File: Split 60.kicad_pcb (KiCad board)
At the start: 2 copper layers, 173 x 106.4 mm, 175 parts, among them SW1 SW_Push, SW2 SW_Push, U1 ATmega32U4-AU, U2 ATmega32U4-AU, Y1 16MHz, Y2 16MHz

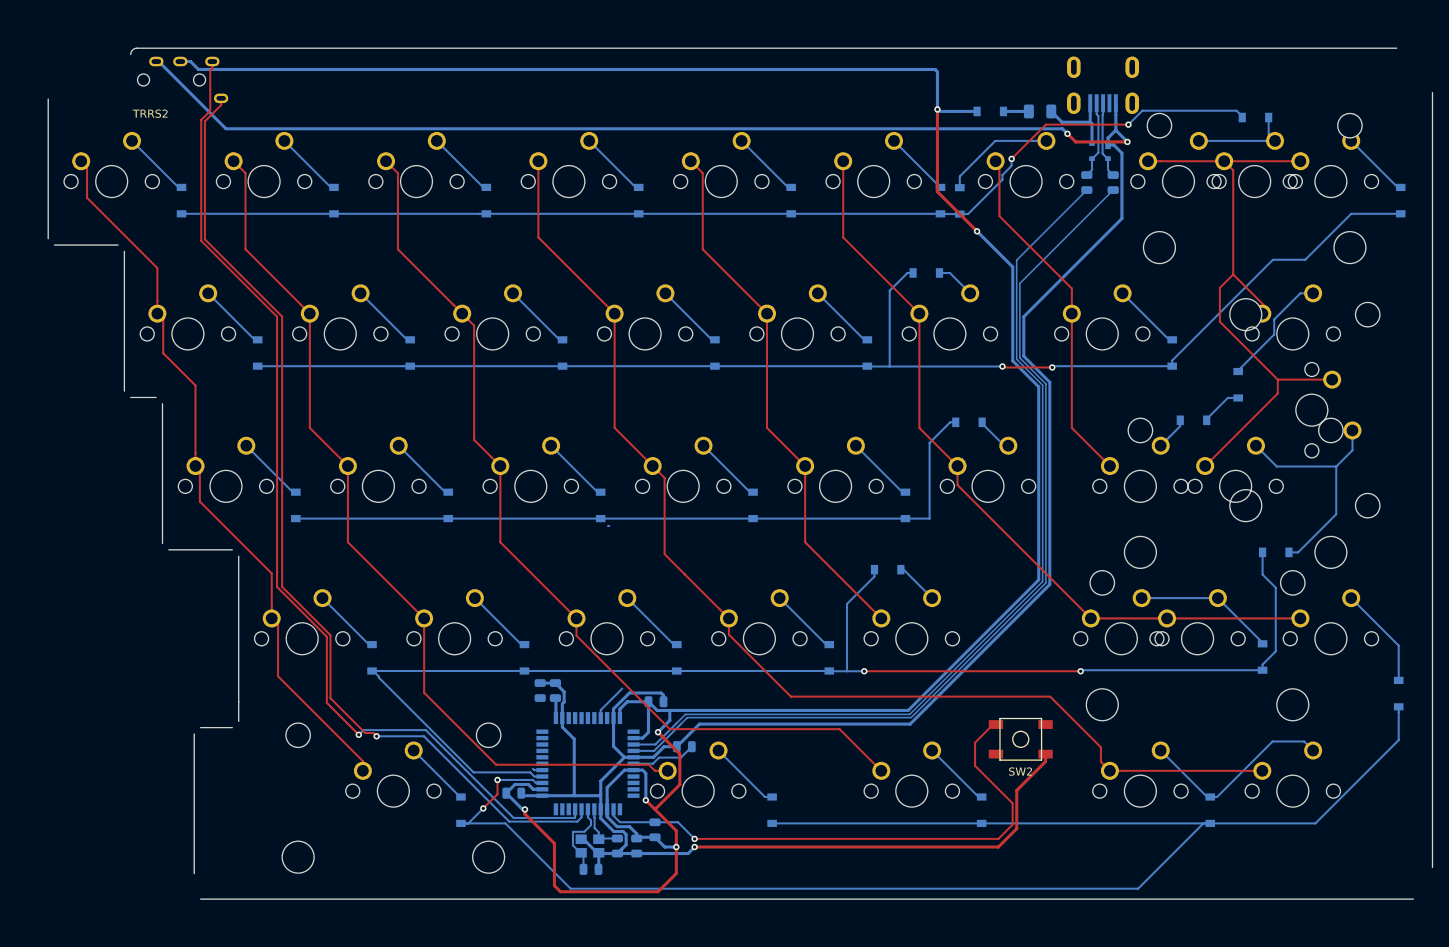
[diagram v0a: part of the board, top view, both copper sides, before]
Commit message: Rename to split 60, tweak routing
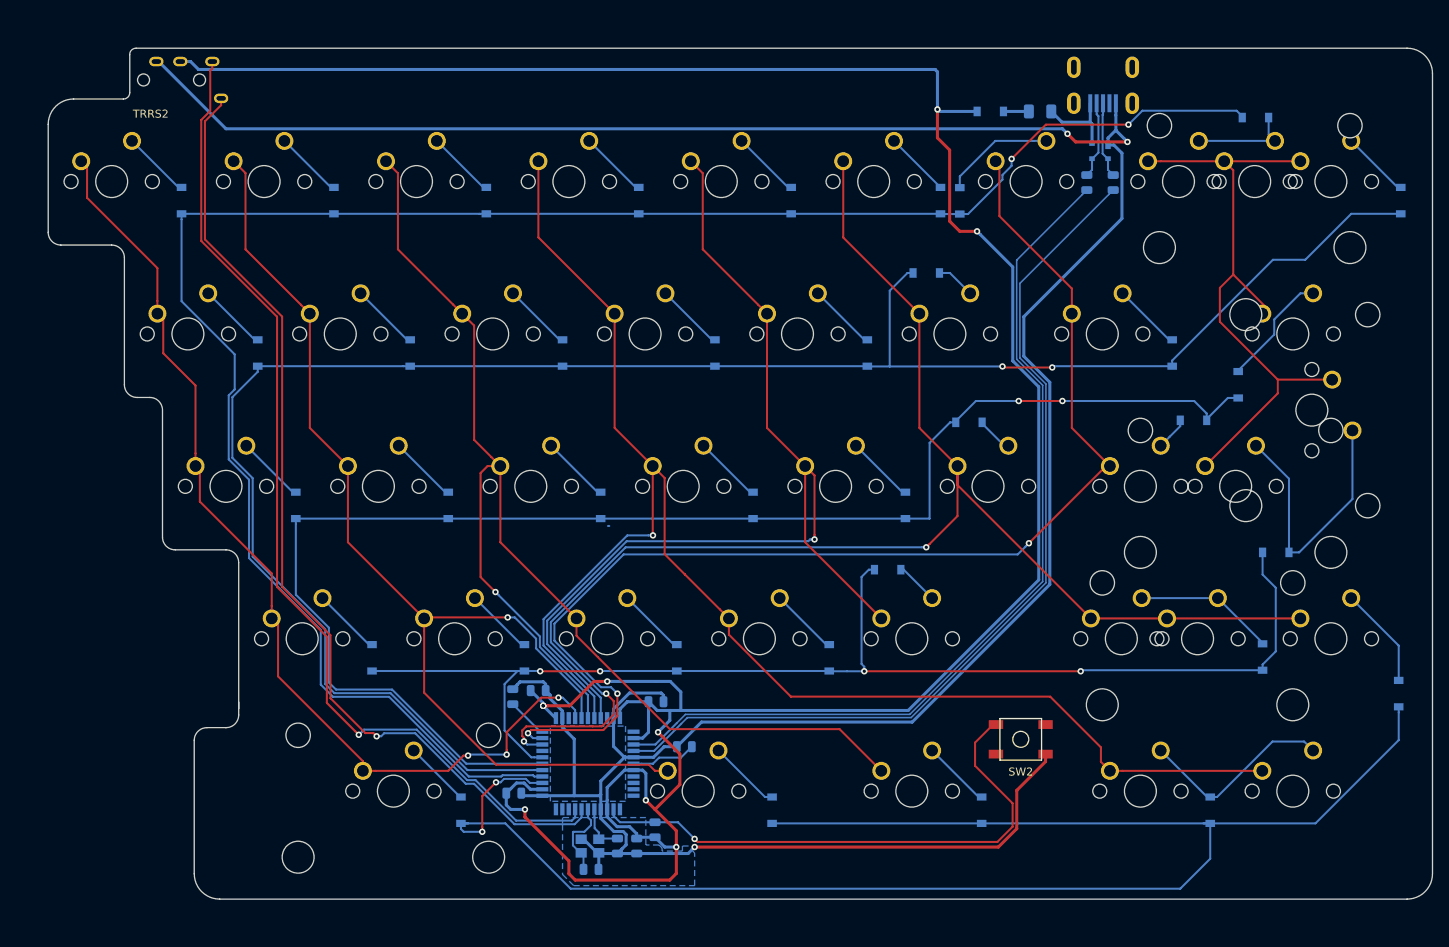
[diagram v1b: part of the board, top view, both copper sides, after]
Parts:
- moved R8 3.51 mm to (317.6, 331.1)
- moved C12 2.16 mm to (320.8, 330.3), turned to 0 degrees
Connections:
- U2 pad 26: R_R3 -> R_R0
- U2 pad 27: R_R2 -> R_R1
- U2 pad 28: R_R1 -> R_R2
- U2 pad 29: R_R0 -> R_R3
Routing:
- net R_C6: track 44.0 -> 151.3 mm, vias 0 -> 3
- net R_R0: track 139.2 -> 238.5 mm
- net R_C5: track 96.2 -> 190.1 mm, vias 0 -> 3
- net R_R2: track 99.4 -> 185.3 mm, vias 0 -> 2
- net R_R1: track 164.6 -> 242.1 mm
- net R_C4: track 71.8 -> 129.3 mm, vias 0 -> 1
- net R_C3: track 143.9 -> 185.6 mm, vias 0 -> 1
- net R_C2: track 114.3 -> 153.3 mm, vias 0 -> 1
- net R_C0: track 90.8 -> 124.4 mm, vias 0 -> 3
- net R_C1: track 110.8 -> 138.2 mm, vias 0 -> 1
- net +5V: track 324.3 -> 347.3 mm, vias 6 -> 9
- net R_R3: track 168.6 -> 156.7 mm, vias 2 -> 4
- net R_R4: track 200.8 -> 208.2 mm
- net Net-(R8-Pad2): track 0.00 -> 5.12 mm
- net Net-(D65-Pad2): track 30.3 -> 34.3 mm
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- added copper zone on B.Cu, net GND
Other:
- outline, holes or cut-outs redrawn
